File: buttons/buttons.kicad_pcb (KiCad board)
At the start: 2 copper layers, 62 x 22.4 mm, 20 parts, among them J1 77311-862-11LF

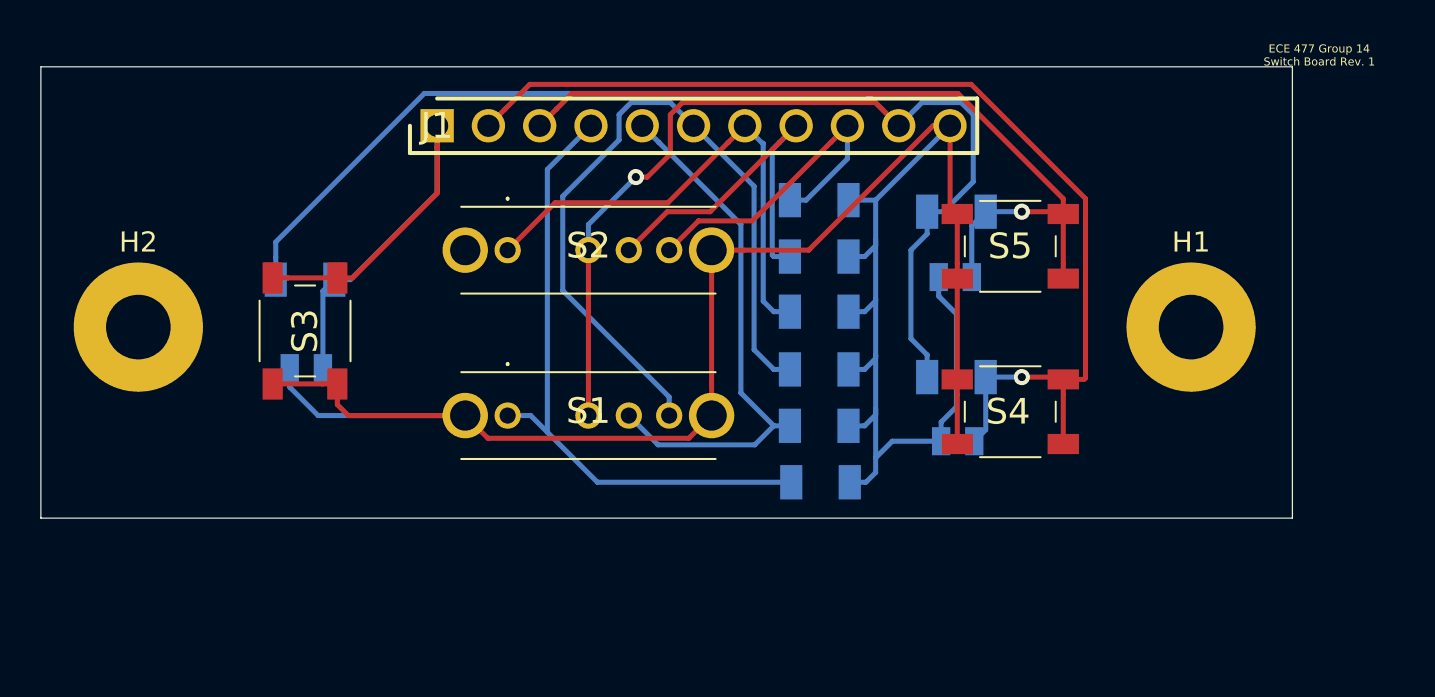
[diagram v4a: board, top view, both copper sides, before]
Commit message: edited main board headers for buttons, daughterboard power
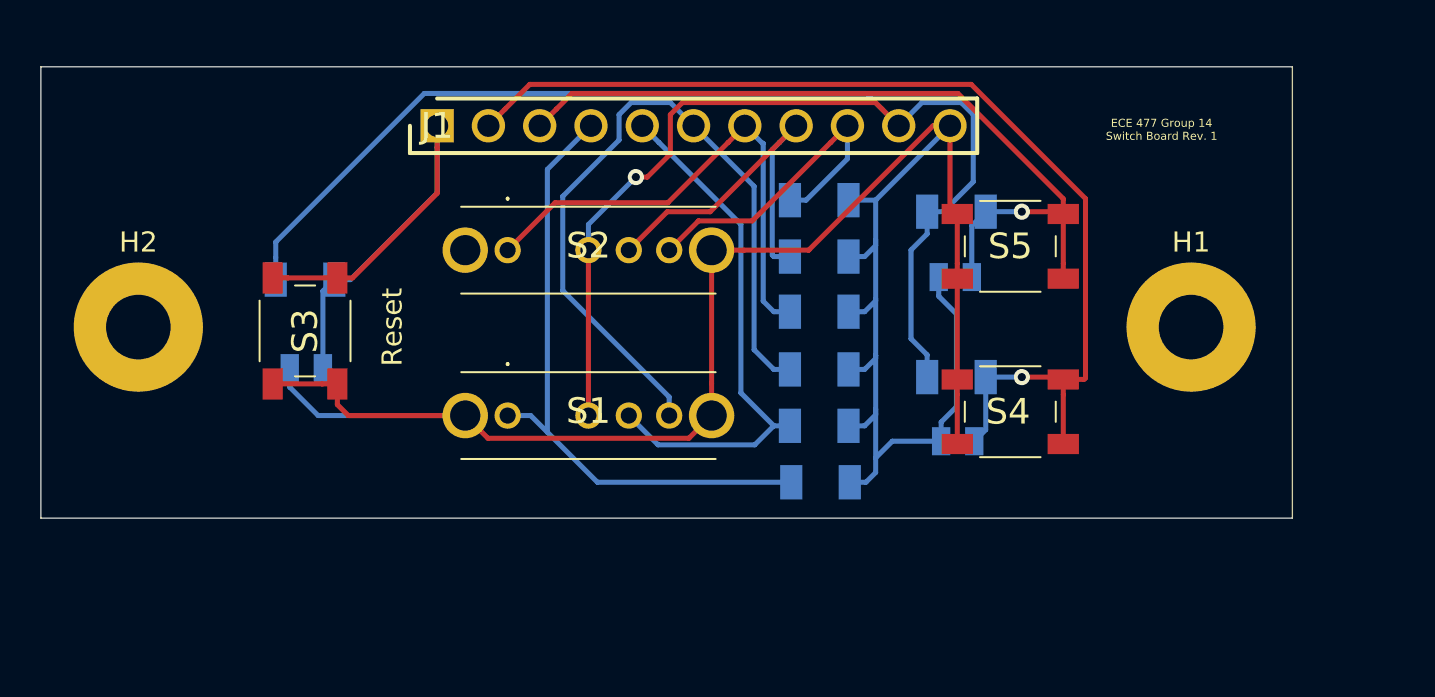
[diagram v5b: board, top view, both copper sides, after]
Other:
- board text added: "Reset"
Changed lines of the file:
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@@
   (general
     (thickness 1.6)
-    (drawings 5)
+    (drawings 6)
     (tracks 178)
     (zones 0)
@@
     )
   )
+  (gr_text Reset (at 107.6325 68.707 90) (layer F.SilkS)
+    (effects (font (size 1 1) (thickness 0.15)))
+  )
   (gr_line (start 152.2095 55.8165) (end 152.2095 78.1685) (layer Edge.Cuts) (width 0.05))
   (gr_line (start 90.2335 55.8165) (end 152.2095 55.8165) (layer Edge.Cuts) (width 0.05))
   (gr_line (start 90.2335 78.1685) (end 90.2335 55.8165) (layer Edge.Cuts) (width 0.05))
   (gr_line (start 152.2095 78.1685) (end 90.2335 78.1685) (layer Edge.Cuts) (width 0.05))
-  (gr_text "ECE 477 Group 14 \nSwitch Board Rev. 1" (at 153.543 55.245) (layer F.SilkS)
+  (gr_text "ECE 477 Group 14 \nSwitch Board Rev. 1" (at 145.7325 58.928) (layer F.SilkS)
     (effects (font (size 0.4 0.4) (thickness 0.1)))
   )

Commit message: gerbers
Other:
- rule pad_to_mask_clearance: 0.051 -> 0
